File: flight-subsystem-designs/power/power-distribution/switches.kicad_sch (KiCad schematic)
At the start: 15 parts, among them U10 LTC1477CS8, U12 LTC1477CS8, U9 LTC1477CS8

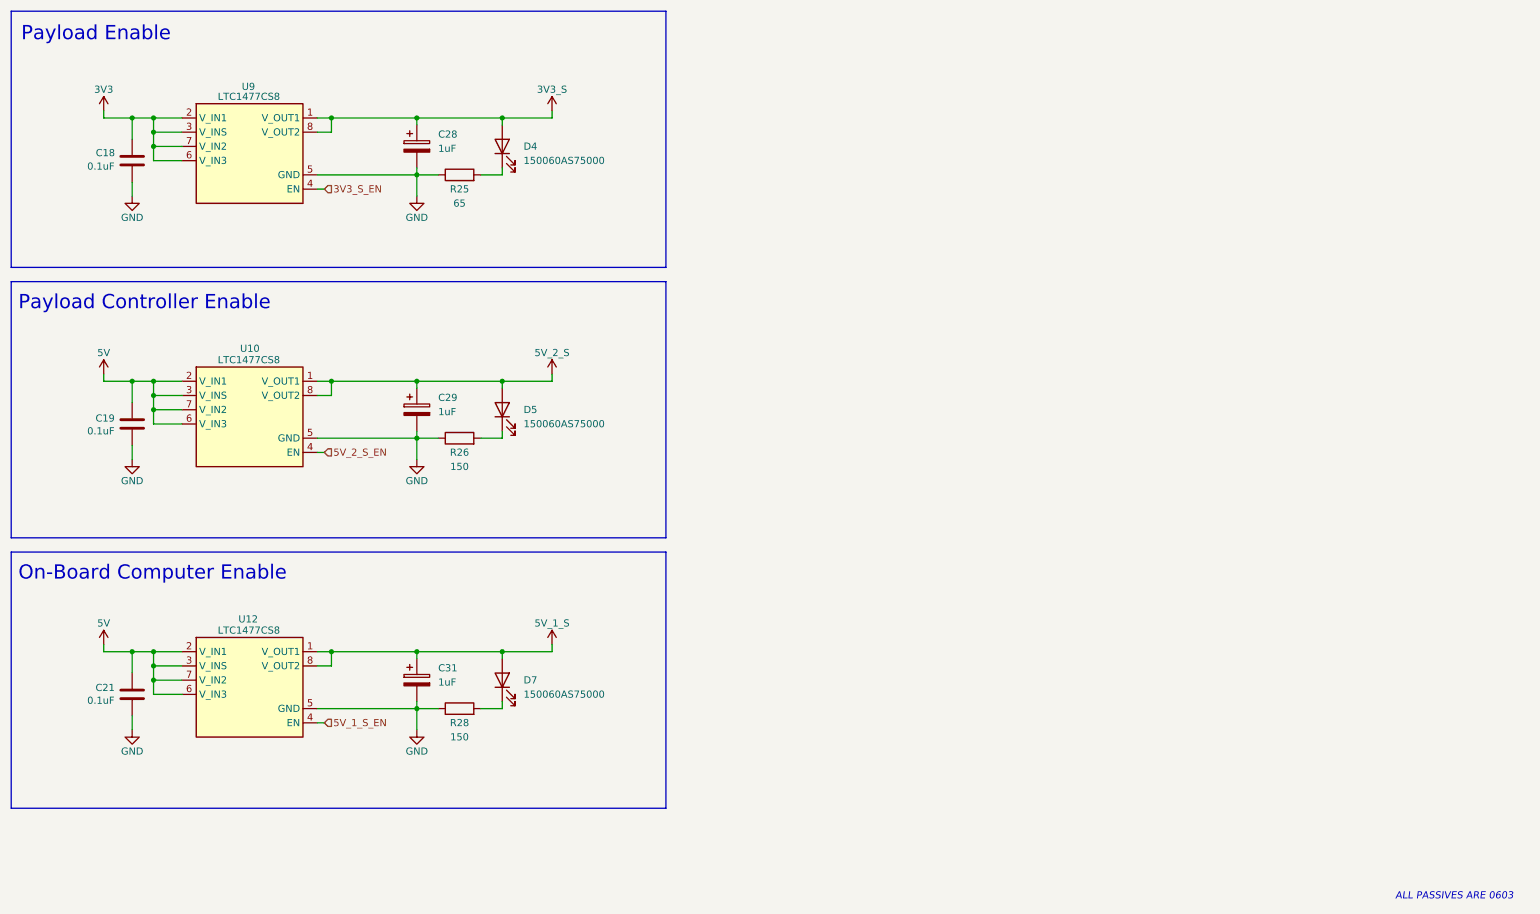
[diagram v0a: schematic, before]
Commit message: feat: PDU 4.0.0 (WIP)
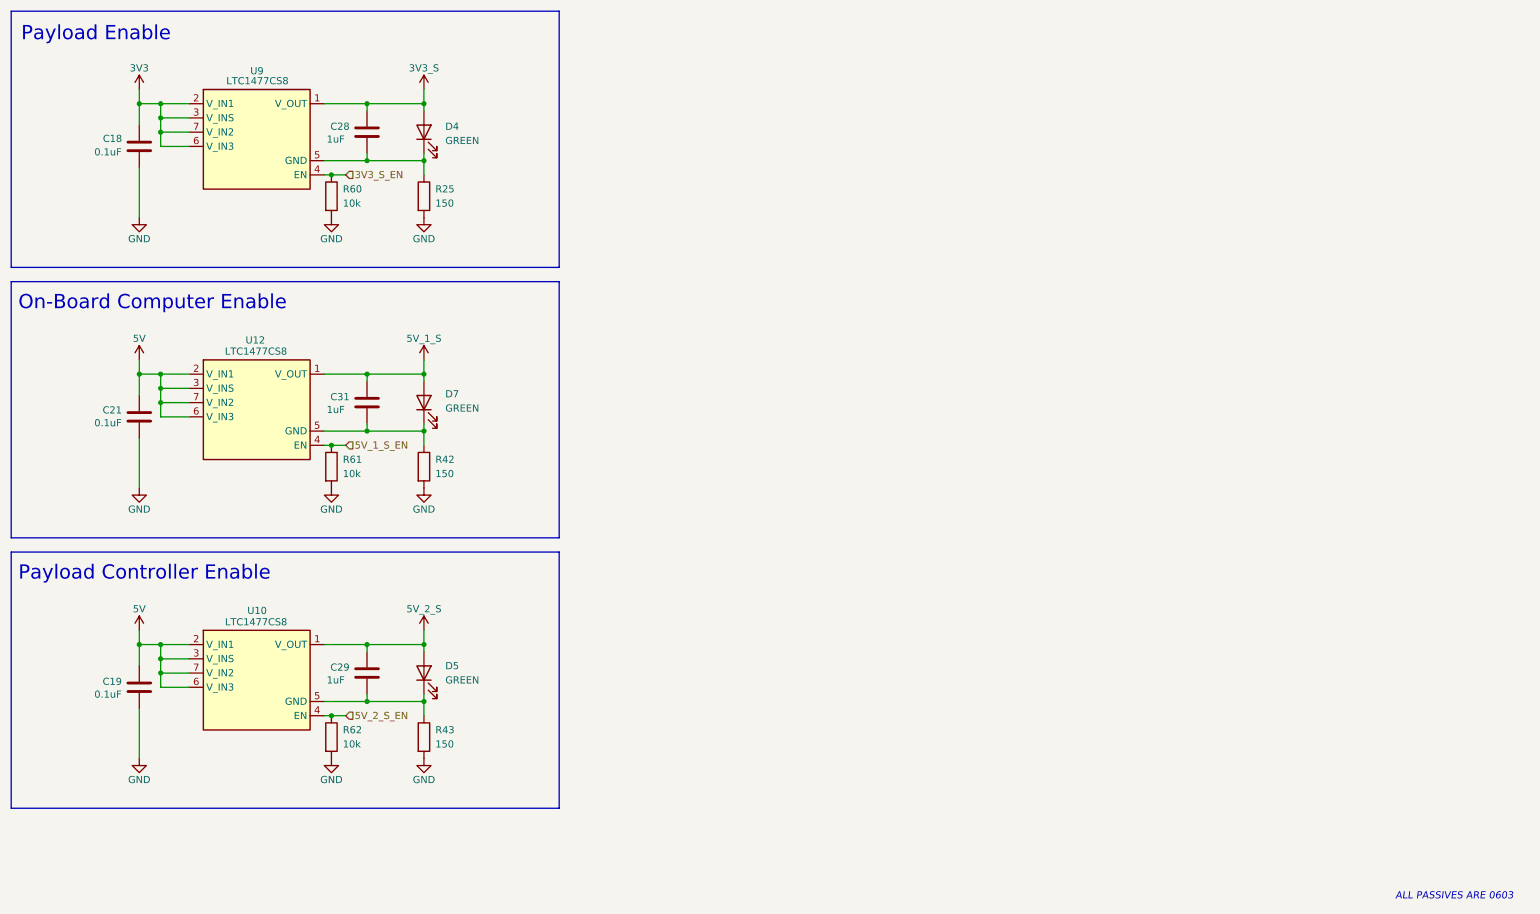
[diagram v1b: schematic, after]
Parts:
- removed C28, C29, C31: 1uF, Capacitor_SMD:C_0603_1608Metric, symbol Device:C_Polarized
- removed R26, R28: 150, Resistor_SMD:R_0603_1608Metric, symbol Device:R
- added C28, C29, C31: 1uF, Capacitor_SMD:C_0603_1608Metric, symbol Device:C
- added R42, R43: 150, Resistor_SMD:R_0603_1608Metric, symbol Device:R
- added R60, R61, R62: 10k, Resistor_SMD:R_0603_1608Metric, symbol Device:R
- D4, D5, D7: value 150060AS75000 -> GREEN
- R25: value 65 -> 150
- U10, U12, U9: symbol pdu:LTC1478 -> pdu:LTC1477CS8
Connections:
- net 3V3_S: now also C28.1
- net 3V3_S_EN: now also R60.1
- net 5V_1_S: now also C31.1
- net 5V_1_S_EN: now also R61.1
- net 5V_2_S: now also C29.1
- net 5V_2_S_EN: now also R62.1
- net GND: now also R25.2, R42.2, R43.2, R60.2, R61.2, R62.2; no longer R25.1, U10.5 (GND), U12.5 (GND), U9.5 (GND)
- net at D5.1 (K): now also U10.5 (GND), C29.2, R43.1
- net at D4.1 (K): now also R25.1, U9.5 (GND), C28.2; no longer R25.2
- net at D7.1 (K): now also U12.5 (GND), C31.2, R42.1
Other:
- moved on the sheet: C18, C19, C21, D4, D5, D7

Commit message: shi
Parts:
- renumbered C21 to C19, C19 to C21, C31 to C29, C29 to C31, D7 to D5, D5 to D7, R60 to R25, R61 to R42, R62 to R43, R25 to R45, R42 to R46, R43 to R50, U12 to U10, U10 to U12
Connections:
- net GND: now also C28.2, C29.2, C31.2, U10.5 (GND), U12.5 (GND), U9.5 (GND)
- net at D5.1 (K), R46.1: no longer C29.2, U10.5 (GND)
- net at D7.1 (K), R50.1: no longer C31.2, U12.5 (GND)
- net at D4.1 (K), R45.1: no longer C28.2, U9.5 (GND)
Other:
- note added: "Batt Heat Enable"
- note removed: "Payload Controller Enable"
- moved on the sheet: D4, D5, D7, R45, R46, R50
